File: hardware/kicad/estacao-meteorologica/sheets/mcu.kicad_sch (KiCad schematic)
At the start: 1 part, among them U5 NUCLEO-F446RE

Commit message: refatoracao: atualizacoes de hardware e falta revisao LoRa
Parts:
- removed U5: NUCLEO-F446RE, myLibrary:MODULE_NUCLEO-F446RE, symbol Hardware_MCU:NUCLEO-F446RE_Morpho
- added BT1: Battery_Cell, symbol Device:Battery_Cell
- added C13, C14, C23, C24, C4, C5: 100n, symbol Device:C
- added C15, C16: 4.7u, symbol Device:C
- added C17: 1u, symbol Device:C
- added C18: 10n, symbol Device:C
- added C19, C20, C21, C22: 15pF, symbol Device:C
- added FB1: FerriteBead, symbol Device:FerriteBead
- added J1: Conn_01x02_Pin, symbol Connector:Conn_01x02_Pin
- added J2: Conn_01x06_Pin, symbol Connector:Conn_01x06_Pin
- added J3: UART DEBUG 3V3, symbol Connector:Conn_01x03_Pin
- added R10, R8: 10k, symbol Device:R
- added R11, R6: 4.7k, symbol Device:R
- added SW1: SW_Push, symbol Switch:SW_Push
- added U4: STM32F446RET6, Package_QFP:LQFP-64_10x10mm_P0.5mm, symbol MCU_ST_STM32F4:STM32F446RETx
- added Y2: Crystal, symbol Device:Crystal
- added Y3: Crystal_GND24, symbol Device:Crystal_GND24
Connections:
- net GND: now also BT1.2 (-), C13.2, C14.2, C15.2, C16.2, C17.2, C18.2, C19.1, C20.1, C21.1, C22.1, C23.2, C24.2, C4.2, C5.2, J2.2 (Pin_2), J3.1 (Pin_1), R10.2, SW1.2, U4.12 (VSSA), U4.18 (VSS), U4.31 (VSS), U4.47 (VSS), U4.63 (VSS), Y3.2, Y3.4
- net Lora_DIO0: now also U4.44 (PA11)
- net Lora_DIO1: now also U4.45 (PA12)
- net Lora_MISO: now also U4.35 (PB14)
- net Lora_MOSI: now also U4.36 (PB15)
- net Lora_NSS: now also U4.33 (PB12)
- net Lora_RST: now also U4.24 (PC4)
- net Lora_SCK: now also U4.34 (PB13)
- net MCU_MOSI: now also U4.23 (PA7)
- net RAIN_PULSE: now also U4.15 (PA1)
- net SD_CS: now also U4.25 (PC5)
- net SD_MISO: now also U4.22 (PA6)
- net SD_SCK: now also U4.21 (PA5)
- net WIND_DIR_ADC: now also U4.14 (PA0)
- net WIND_SPEED_PULSE: now also U4.38 (PC7)
- new net: C22.2, U4.4 (PC15), Y2.1
- new net: C21.2, U4.3 (PC14), Y2.2
- new net: C19.2, U4.5 (PH0), Y3.1
- new net: C20.2, U4.6 (PH1), Y3.3
- new net: C16.1, U4.30 (VCAP_1)
- new net +3V3: C13.1, C14.1, C15.1, C4.1, C5.1, FB1.1, J1.1 (Pin_1), J2.1 (Pin_1), R11.1, R6.1, R8.1, U4.19 (VDD), U4.32 (VDD), U4.48 (VDD), U4.64 (VDD)
- new net BOOT0: J1.2 (Pin_2), R10.1, U4.60 (BOOT0)
- new net DHT_SIG: U4.41 (PA8)
- new net I2C1_SCL: R6.2, U4.58 (PB6)
- new net I2C1_SDA: R11.2, U4.59 (PB7)
- new net NRST: C24.1, J2.5 (Pin_5), R8.2, SW1.1, U4.7 (NRST)
- new net RXD: J3.3 (Pin_3), U4.17 (PA3)
- new net SWCLK: J2.4 (Pin_4), U4.49 (PA14)
- new net SWDIO: J2.3 (Pin_3), U4.46 (PA13)
- new net SWO: J2.6 (Pin_6), U4.55 (PB3)
- new net TXD: J3.2 (Pin_2), U4.16 (PA2)
- new net VBAT: BT1.1 (+), C23.1, U4.1 (VBAT)
- new net VDDA: C17.1, C18.1, FB1.2, U4.13 (VDDA)
- no-connect marks 42 -> 24

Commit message: refatoracao: lora + Verificacao projeto inteiro
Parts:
- BT1: value Battery_Cell -> CR2032 / BS-5 vertical; footprint (none) -> Hardware_MCU:BT_Holder_MPD_BS-5_Vertical; Assembly (none) -> Manual — suporte PTH vertical.; Electrical Parameters (none) -> CR2032/BR2032, 3 V; THT; 3 furos Ø0,9 mm; dois pads + e um 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; Function (none) -> Alimenta VBAT do STM32 para reter o domínio de backup e o R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; LCSC (none) -> C6869743; LCSC Part (none) -> C6869743; MPN (none) -> BS-5; Manufacturer (none) -> MPD (Memory Protection Devices); Modelo 3D (none) -> ${KIPRJMOD}/../../libraries/Hardware_MCU/Hardware_MCU.3dsha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; Status_Ficha (none) -> Conferido com desenho mecânico e STEP oficial do MPD BS-5. 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
- C13, C14, C23, C24, C4, C5: footprint (none) -> Capacitor_SMD:C_0603_1608Metric; LCSC (none) -> C14663; LCSC Part (none) -> C14663; MPN (none) -> CC0603KRX7R9BB104; Manufacturer (none) -> YAGEO; Modelo 3D (none) -> ${KICAD9_3DMODEL_DIR}/Capacitor_SMD.3dshapes/C_0603_1608Met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; Status_Ficha (none) -> Conferido no catalogo em 2026-09-24; verificar estoque ao c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
- C15, C16: footprint (none) -> Capacitor_SMD:C_0805_2012Metric; LCSC (none) -> C7307475; LCSC Part (none) -> C7307475; MPN (none) -> MSAST21GAB5475MTNA01; Manufacturer (none) -> Taiyo Yuden; Modelo 3D (none) -> ${KICAD9_3DMODEL_DIR}/Capacitor_SMD.3dshapes/C_0805_2012Met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; Status_Ficha (none) -> Conferido no catalogo em 2026-09-24; verificar estoque ao c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
- C17: footprint (none) -> Capacitor_SMD:C_0603_1608Metric; LCSC (none) -> C513775; LCSC Part (none) -> C513775; MPN (none) -> CS1608X7R105K250NRB; Manufacturer (none) -> Samwha Capacitor; Modelo 3D (none) -> ${KICAD9_3DMODEL_DIR}/Capacitor_SMD.3dshapes/C_0603_1608Met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; Status_Ficha (none) -> Conferido no catalogo em 2026-09-24; verificar estoque ao c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
- C18: footprint (none) -> Capacitor_SMD:C_0603_1608Metric; LCSC (none) -> C57112; LCSC Part (none) -> C57112; MPN (none) -> 0603B103K500NT; Manufacturer (none) -> FH (Guangdong Fenghua Advanced Tech); Modelo 3D (none) -> ${KICAD9_3DMODEL_DIR}/Capacitor_SMD.3dshapes/C_0603_1608Met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; Status_Ficha (none) -> Conferido no catalogo em 2026-09-24; verificar estoque ao c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
- C19: footprint (none) -> Capacitor_SMD:C_0603_1608Metric; Function (none) -> Capacitor de carga do HSE, entre PH0/OSC_IN e GND.; LCSC (none) -> C107037; LCSC Part (none) -> C107037; MPN (none) -> CC0603JRNPO9BN150; Manufacturer (none) -> YAGEO; Modelo 3D (none) -> ${KICAD9_3DMODEL_DIR}/Capacitor_SMD.3dshapes/C_0603_1608Met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; Status_Ficha (none) -> Conferido com Y3: 15 pF C0G, em par simétrico com C20 para 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
- C20: footprint (none) -> Capacitor_SMD:C_0603_1608Metric; Function (none) -> Capacitor de carga do HSE, entre PH1/OSC_OUT e GND.; LCSC (none) -> C107037; LCSC Part (none) -> C107037; MPN (none) -> CC0603JRNPO9BN150; Manufacturer (none) -> YAGEO; Modelo 3D (none) -> ${KICAD9_3DMODEL_DIR}/Capacitor_SMD.3dshapes/C_0603_1608Met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; Status_Ficha (none) -> Conferido com Y3: 15 pF C0G, em par simétrico com C19 para 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
- C21: value 15pF -> 9pF; footprint (none) -> Capacitor_SMD:C_0603_1608Metric; Function (none) -> Capacitor de carga do LSE, entre PC14/OSC32_IN e GND.; LCSC (none) -> C3877909; LCSC Part (none) -> C3877909; MPN (none) -> AC0603DRNPO9BN9R0; Manufacturer (none) -> YAGEO; Modelo 3D (none) -> ${KICAD9_3DMODEL_DIR}/Capacitor_SMD.3dshapes/C_0603_1608Met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; Status_Ficha (none) -> Escolhido para Y2 de CL 7 pF: C21=C22=9 pF com cerca de 2,5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
- C22: value 15pF -> 9pF; footprint (none) -> Capacitor_SMD:C_0603_1608Metric; Function (none) -> Capacitor de carga do LSE, entre PC15/OSC32_OUT e GND.; LCSC (none) -> C3877909; LCSC Part (none) -> C3877909; MPN (none) -> AC0603DRNPO9BN9R0; Manufacturer (none) -> YAGEO; Modelo 3D (none) -> ${KICAD9_3DMODEL_DIR}/Capacitor_SMD.3dshapes/C_0603_1608Met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; Status_Ficha (none) -> Escolhido para Y2 de CL 7 pF: C21=C22=9 pF com cerca de 2,5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
- FB1: footprint (none) -> Inductor_SMD:L_0603_1608Metric; LCSC (none) -> C14709; LCSC Part (none) -> C14709; MPN (none) -> BLM18PG121SN1D; Manufacturer (none) -> Murata Electronics; Modelo 3D (none) -> ${KICAD9_3DMODEL_DIR}/Inductor_SMD.3dshapes/L_0603_1608Metr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; Status_Ficha (none) -> Conferido no catalogo em 2026-09-24; verificar estoque ao c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
- J1: footprint (none) -> Connector_PinHeader_2.54mm:PinHeader_1x02_P2.54mm_Vertical; Assembly (none) -> Manual - pin header PTH 2,54 mm; LCSC (none) -> C492401; LCSC Part (none) -> C492401; MPN (none) -> PZ254V-11-02P; Manufacturer (none) -> XFCN; Modelo 3D (none) -> ${KICAD9_3DMODEL_DIR}/Connector_PinHeader_2.54mm.3dshapes/P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; Status_Ficha (none) -> Conferido no catalogo em 2026-09-24; verificar estoque ao c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
- J2: footprint (none) -> Connector_PinHeader_2.54mm:PinHeader_1x06_P2.54mm_Vertical; Assembly (none) -> Manual - pin header PTH 2,54 mm; LCSC (none) -> C492405; LCSC Part (none) -> C492405; MPN (none) -> PZ254V-11-06P; Manufacturer (none) -> XFCN; Modelo 3D (none) -> ${KICAD9_3DMODEL_DIR}/Connector_PinHeader_2.54mm.3dshapes/P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; Status_Ficha (none) -> Conferido no catalogo em 2026-09-24; verificar estoque ao c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
- J3: footprint (none) -> Connector_PinHeader_2.54mm:PinHeader_1x03_P2.54mm_Vertical; Assembly (none) -> Manual - pin header PTH 2,54 mm; LCSC (none) -> C492402; LCSC Part (none) -> C492402; MPN (none) -> PZ254V-11-03P; Manufacturer (none) -> XFCN; Modelo 3D (none) -> ${KICAD9_3DMODEL_DIR}/Connector_PinHeader_2.54mm.3dshapes/P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; Status_Ficha (none) -> Conferido no catalogo em 2026-09-24; verificar estoque ao c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
- R10, R8: footprint (none) -> Resistor_SMD:R_0603_1608Metric; LCSC (none) -> C25804; LCSC Part (none) -> C25804; MPN (none) -> 0603WAF1002T5E; Manufacturer (none) -> UNI-ROYAL(Uniroyal Elec); Modelo 3D (none) -> ${KICAD9_3DMODEL_DIR}/Resistor_SMD.3dshapes/R_0603_1608Metr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; Status_Ficha (none) -> Conferido no catalogo em 2026-09-24; verificar estoque ao c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
- R11, R6: footprint (none) -> Resistor_SMD:R_0603_1608Metric; LCSC (none) -> C23162; LCSC Part (none) -> C23162; MPN (none) -> 0603WAF4701T5E; Manufacturer (none) -> UNI-ROYAL(Uniroyal Elec); Modelo 3D (none) -> ${KICAD9_3DMODEL_DIR}/Resistor_SMD.3dshapes/R_0603_1608Metr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; Status_Ficha (none) -> Conferido no catalogo em 2026-09-24; verificar estoque ao c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
- SW1: footprint (none) -> Button_Switch_SMD:SW_SPST_TL3342; LCSC (none) -> C2886898; LCSC Part (none) -> C2886898; MPN (none) -> TL3342F160QG; Manufacturer (none) -> E-Switch; Modelo 3D (none) -> ${KICAD9_3DMODEL_DIR}/Button_Switch_SMD.3dshapes/SW_SPST_TL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; Status_Ficha (none) -> Conferido no catalogo em 2026-09-24; verificar estoque ao c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
- U4: LCSC (none) -> C69336; LCSC Part (none) -> C69336; MPN (none) -> STM32F446RET6; Manufacturer (none) -> STMicroelectronics; Modelo 3D (none) -> ${KICAD9_3DMODEL_DIR}/Package_QFP.3dshapes/LQFP-64_10x10mm_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; Status_Ficha (none) -> Conferido no catalogo em 2026-09-24; verificar estoque ao c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
- Y2: value Crystal -> 32.768 kHz / CL 7 pF; footprint (none) -> Crystal:Crystal_SMD_3215-2Pin_3.2x1.5mm; Electrical Parameters (none) -> 32,768 kHz; CL 7 pF; ±20 ppm; SMD3215-2P.; Fabricante / MPN (none) -> SJK (Shenzhen Crystal Tech) / 7LC32768F07UC; Function (none) -> Referência LSE de baixo consumo do RTC do STM32F446, mantid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; LCSC (none) -> C252399; LCSC Part (none) -> C252399; MPN (none) -> 7LC32768F07UC; Manufacturer (none) -> SJK (Shenzhen Crystal Tech); Modelo 3D (none) -> ${KICAD9_3DMODEL_DIR}/Crystal.3dshapes/Crystal_SMD_3215-2Pi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; Status_Ficha (none) -> Conferido. C21=C22=9 pF visa CL≈7 pF para capacitância para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
- Y3: value Crystal_GND24 -> 8 MHz / CL 10 pF; footprint (none) -> Crystal:Crystal_SMD_3225-4Pin_3.2x2.5mm; Electrical Parameters (none) -> 8 MHz; CL 10 pF; ±10 ppm; SMD3225-4P.; Fabricante / MPN (none) -> Suzhou Liming Elec / 3225-8.00-10-10-10/A; Function (none) -> Referência HSE do STM32F446 (PH0/OSC_IN e PH1/OSC_OUT).; LCSC (none) -> C518154; LCSC Part (none) -> C518154; MPN (none) -> 3225-8.00-10-10-10/A; Manufacturer (none) -> Suzhou Liming Elec; Modelo 3D (none) -> ${KICAD9_3DMODEL_DIR}/Crystal.3dshapes/Crystal_SMD_3225-4Pi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; Status_Ficha (none) -> Conferido. Com C19=C20=15 pF e cerca de 2,5 pF de parasitas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
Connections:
- net Lora_DIO2: now reaches U4.26 (PB0)
- no-connect marks 24 -> 23

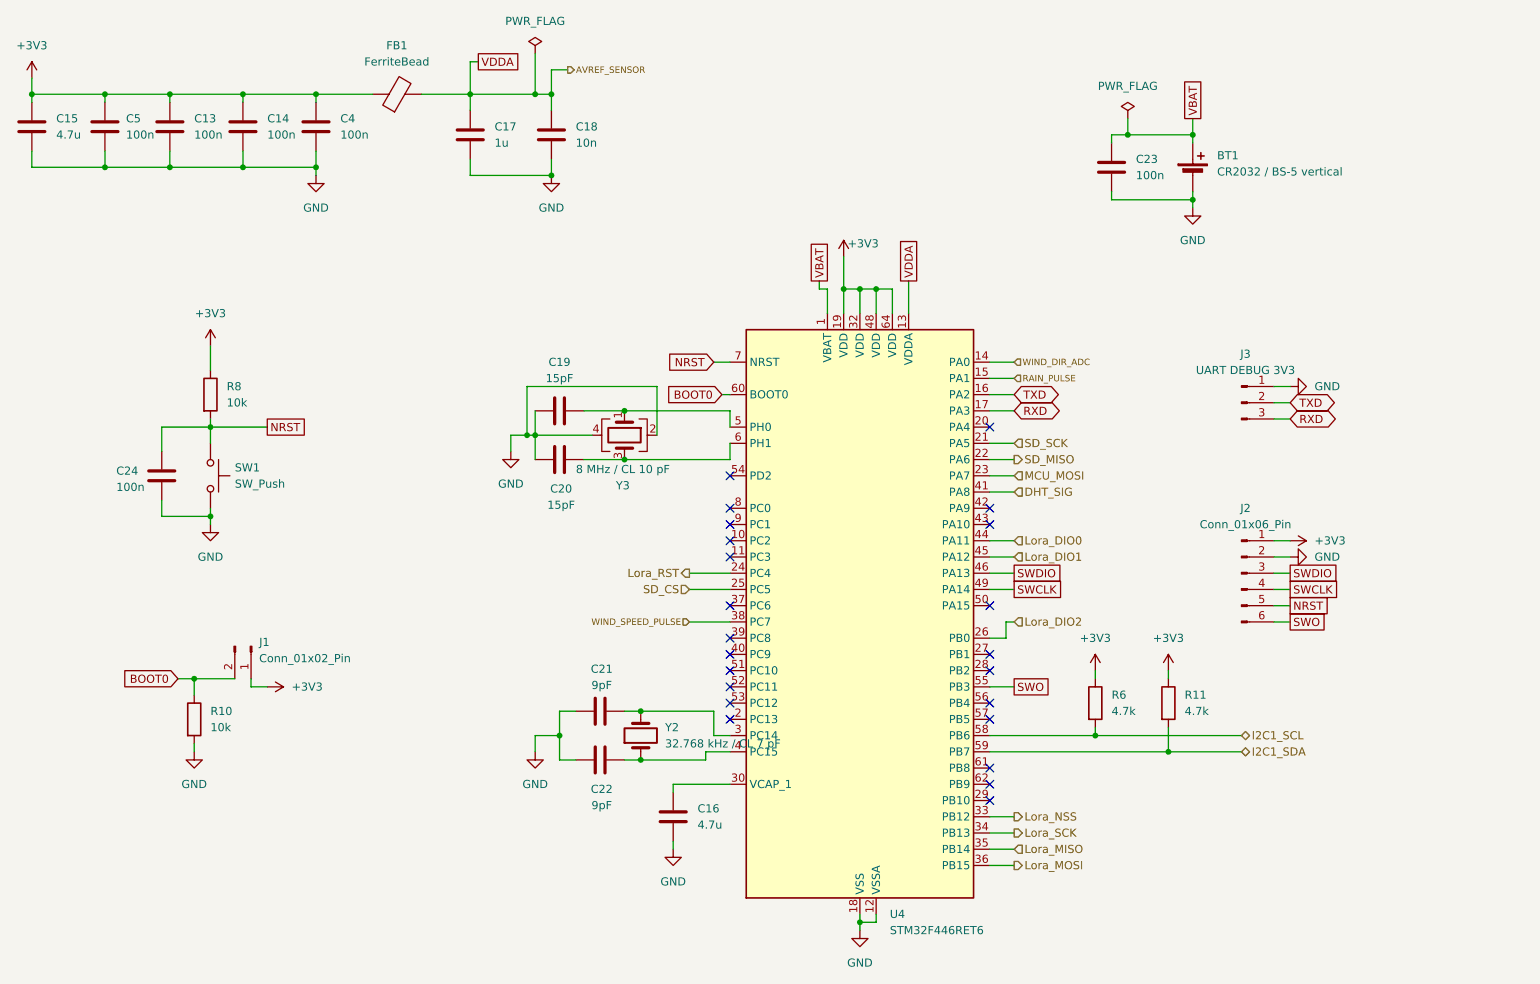
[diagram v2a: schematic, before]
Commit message: Padronizacao de nomes e numero de componentes
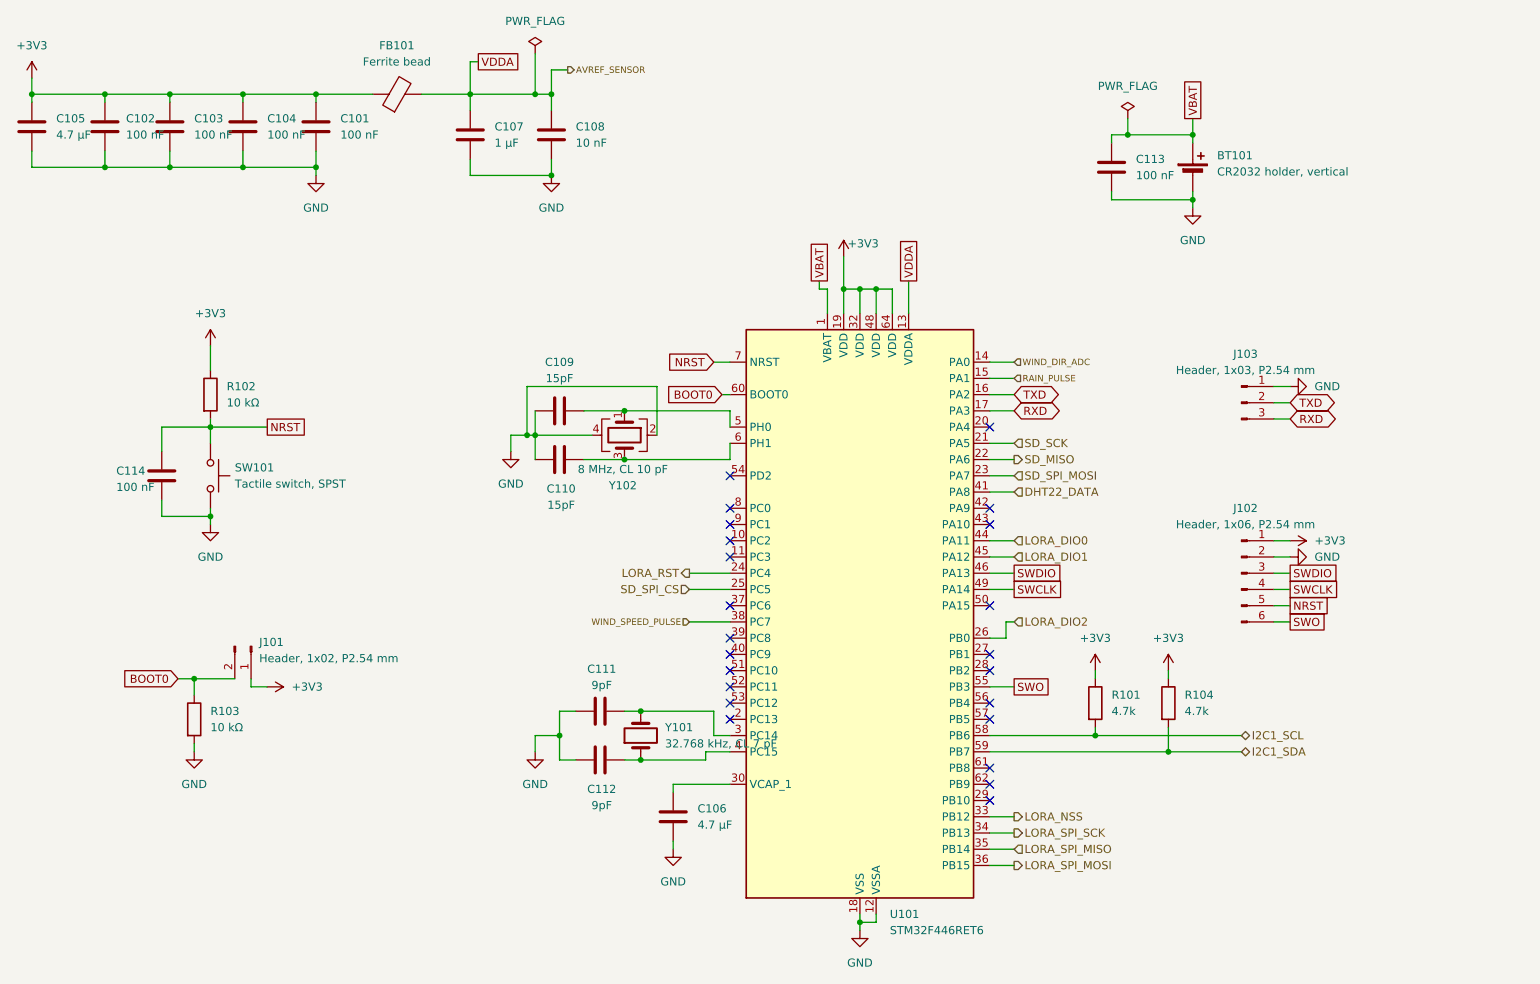
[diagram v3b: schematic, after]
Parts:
- BT101: renamed from BT1; value CR2032 / BS-5 vertical -> CR2032 holder, vertical; Electrical Parameters CR2032/BR2032, 3 V; THT; 3 furos Ø0,9 mm; dois pads + e um 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 -> (none); LCSC Part C6869743 -> (none); Modelo 3D ${KIPRJMOD}/../../libraries/Hardware_MCU/Hardware_MCU.3dsha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 -> (none); Specification (none) -> CR2032/BR2032, 3 V; THT; 3 furos Ø0,9 mm; dois pads + e um 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; Status_Ficha Conferido com desenho mecânico e STEP oficial do MPD BS-5. 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 -> (none); Verification (none) -> Conferido com desenho mecânico e STEP oficial do MPD BS-5. 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
- C101: renamed from C4; value 100n -> 100 nF; Assembly (none) -> SMT; Function (none) -> Capacitor de desacoplamento ou filtro local.; LCSC Part C14663 -> (none); Modelo 3D ${KICAD9_3DMODEL_DIR}/Capacitor_SMD.3dshapes/C_0603_1608Met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 -> (none); Specification (none) -> 100 nF; Status_Ficha Conferido no catalogo em 2026-09-24; verificar estoque ao c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 -> (none); Verification (none) -> Conferido no catalogo em 2026-09-24; verificar estoque ao c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
- C102: renamed from C5; value 100n -> 100 nF; Assembly (none) -> SMT; Function (none) -> Capacitor de desacoplamento ou filtro local.; LCSC Part C14663 -> (none); Modelo 3D ${KICAD9_3DMODEL_DIR}/Capacitor_SMD.3dshapes/C_0603_1608Met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 -> (none); Specification (none) -> 100 nF; Status_Ficha Conferido no catalogo em 2026-09-24; verificar estoque ao c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 -> (none); Verification (none) -> Conferido no catalogo em 2026-09-24; verificar estoque ao c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
- C103: renamed from C13; value 100n -> 100 nF; Assembly (none) -> SMT; Function (none) -> Capacitor de desacoplamento ou filtro local.; LCSC Part C14663 -> (none); Modelo 3D ${KICAD9_3DMODEL_DIR}/Capacitor_SMD.3dshapes/C_0603_1608Met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 -> (none); Specification (none) -> 100 nF; Status_Ficha Conferido no catalogo em 2026-09-24; verificar estoque ao c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 -> (none); Verification (none) -> Conferido no catalogo em 2026-09-24; verificar estoque ao c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
- C104: renamed from C14; value 100n -> 100 nF; Assembly (none) -> SMT; Function (none) -> Capacitor de desacoplamento ou filtro local.; LCSC Part C14663 -> (none); Modelo 3D ${KICAD9_3DMODEL_DIR}/Capacitor_SMD.3dshapes/C_0603_1608Met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 -> (none); Specification (none) -> 100 nF; Status_Ficha Conferido no catalogo em 2026-09-24; verificar estoque ao c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 -> (none); Verification (none) -> Conferido no catalogo em 2026-09-24; verificar estoque ao c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
- C105: renamed from C15; value 4.7u -> 4.7 µF; Assembly (none) -> SMT; Function (none) -> Capacitor de desacoplamento ou filtro local.; LCSC Part C7307475 -> (none); Modelo 3D ${KICAD9_3DMODEL_DIR}/Capacitor_SMD.3dshapes/C_0805_2012Met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 -> (none); Specification (none) -> 4.7 µF; Status_Ficha Conferido no catalogo em 2026-09-24; verificar estoque ao c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 -> (none); Verification (none) -> Conferido no catalogo em 2026-09-24; verificar estoque ao c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
- C106: renamed from C16; value 4.7u -> 4.7 µF; Assembly (none) -> SMT; Function (none) -> Capacitor de desacoplamento ou filtro local.; LCSC Part C7307475 -> (none); Modelo 3D ${KICAD9_3DMODEL_DIR}/Capacitor_SMD.3dshapes/C_0805_2012Met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 -> (none); Specification (none) -> 4.7 µF; Status_Ficha Conferido no catalogo em 2026-09-24; verificar estoque ao c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 -> (none); Verification (none) -> Conferido no catalogo em 2026-09-24; verificar estoque ao c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
- C107: renamed from C17; value 1u -> 1 µF; Assembly (none) -> SMT; Function (none) -> Capacitor de desacoplamento ou filtro local.; LCSC Part C513775 -> (none); Modelo 3D ${KICAD9_3DMODEL_DIR}/Capacitor_SMD.3dshapes/C_0603_1608Met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 -> (none); Specification (none) -> 1 µF; Status_Ficha Conferido no catalogo em 2026-09-24; verificar estoque ao c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 -> (none); Verification (none) -> Conferido no catalogo em 2026-09-24; verificar estoque ao c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
- C108: renamed from C18; value 10n -> 10 nF; Assembly (none) -> SMT; Function (none) -> Capacitor de desacoplamento ou filtro local.; LCSC Part C57112 -> (none); Modelo 3D ${KICAD9_3DMODEL_DIR}/Capacitor_SMD.3dshapes/C_0603_1608Met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 -> (none); Specification (none) -> 10 nF; Status_Ficha Conferido no catalogo em 2026-09-24; verificar estoque ao c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 -> (none); Verification (none) -> Conferido no catalogo em 2026-09-24; verificar estoque ao c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
- C109: renamed from C19; Assembly (none) -> SMT; LCSC Part C107037 -> (none); Modelo 3D ${KICAD9_3DMODEL_DIR}/Capacitor_SMD.3dshapes/C_0603_1608Met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 -> (none); Specification (none) -> 15pF; Status_Ficha Conferido com Y3: 15 pF C0G, em par simétrico com C20 para 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 -> (none); Verification (none) -> Conferido com Y3: 15 pF C0G, em par simétrico com C20 para 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
- C110: renamed from C20; Assembly (none) -> SMT; LCSC Part C107037 -> (none); Modelo 3D ${KICAD9_3DMODEL_DIR}/Capacitor_SMD.3dshapes/C_0603_1608Met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 -> (none); Specification (none) -> 15pF; Status_Ficha Conferido com Y3: 15 pF C0G, em par simétrico com C19 para 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 -> (none); Verification (none) -> Conferido com Y3: 15 pF C0G, em par simétrico com C19 para 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
- C111: renamed from C21; Assembly (none) -> SMT; LCSC Part C3877909 -> (none); Modelo 3D ${KICAD9_3DMODEL_DIR}/Capacitor_SMD.3dshapes/C_0603_1608Met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 -> (none); Specification (none) -> 9pF; Status_Ficha Escolhido para Y2 de CL 7 pF: C21=C22=9 pF com cerca de 2,5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 -> (none); Verification (none) -> Escolhido para Y2 de CL 7 pF: C21=C22=9 pF com cerca de 2,5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
- C112: renamed from C22; Assembly (none) -> SMT; LCSC Part C3877909 -> (none); Modelo 3D ${KICAD9_3DMODEL_DIR}/Capacitor_SMD.3dshapes/C_0603_1608Met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 -> (none); Specification (none) -> 9pF; Status_Ficha Escolhido para Y2 de CL 7 pF: C21=C22=9 pF com cerca de 2,5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 -> (none); Verification (none) -> Escolhido para Y2 de CL 7 pF: C21=C22=9 pF com cerca de 2,5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
- C113: renamed from C23; value 100n -> 100 nF; Assembly (none) -> SMT; Function (none) -> Capacitor de desacoplamento ou filtro local.; LCSC Part C14663 -> (none); Modelo 3D ${KICAD9_3DMODEL_DIR}/Capacitor_SMD.3dshapes/C_0603_1608Met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 -> (none); Specification (none) -> 100 nF; Status_Ficha Conferido no catalogo em 2026-09-24; verificar estoque ao c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 -> (none); Verification (none) -> Conferido no catalogo em 2026-09-24; verificar estoque ao c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
- C114: renamed from C24; value 100n -> 100 nF; Assembly (none) -> SMT; Function (none) -> Capacitor de desacoplamento ou filtro local.; LCSC Part C14663 -> (none); Modelo 3D ${KICAD9_3DMODEL_DIR}/Capacitor_SMD.3dshapes/C_0603_1608Met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 -> (none); Specification (none) -> 100 nF; Status_Ficha Conferido no catalogo em 2026-09-24; verificar estoque ao c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 -> (none); Verification (none) -> Conferido no catalogo em 2026-09-24; verificar estoque ao c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
- FB101: renamed from FB1; value FerriteBead -> Ferrite bead; Assembly (none) -> SMT; Function (none) -> Filtro de ferrite na alimentação.; LCSC Part C14709 -> (none); Modelo 3D ${KICAD9_3DMODEL_DIR}/Inductor_SMD.3dshapes/L_0603_1608Metr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 -> (none); Specification (none) -> Ferrite bead; Status_Ficha Conferido no catalogo em 2026-09-24; verificar estoque ao c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 -> (none); Verification (none) -> Conferido no catalogo em 2026-09-24; verificar estoque ao c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
- J101: renamed from J1; value Conn_01x02_Pin -> Header, 1x02, P2.54 mm; Function (none) -> Conector de interface.; LCSC Part C492401 -> (none); Modelo 3D ${KICAD9_3DMODEL_DIR}/Connector_PinHeader_2.54mm.3dshapes/P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 -> (none); Specification (none) -> Header, 1x02, P2.54 mm; Status_Ficha Conferido no catalogo em 2026-09-24; verificar estoque ao c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 -> (none); Verification (none) -> Conferido no catalogo em 2026-09-24; verificar estoque ao c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
- J102: renamed from J2; value Conn_01x06_Pin -> Header, 1x06, P2.54 mm; Function (none) -> Conector de interface.; LCSC Part C492405 -> (none); Modelo 3D ${KICAD9_3DMODEL_DIR}/Connector_PinHeader_2.54mm.3dshapes/P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 -> (none); Specification (none) -> Header, 1x06, P2.54 mm; Status_Ficha Conferido no catalogo em 2026-09-24; verificar estoque ao c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 -> (none); Verification (none) -> Conferido no catalogo em 2026-09-24; verificar estoque ao c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
- J103: renamed from J3; value UART DEBUG 3V3 -> Header, 1x03, P2.54 mm; Function (none) -> Conector de interface.; LCSC Part C492402 -> (none); Modelo 3D ${KICAD9_3DMODEL_DIR}/Connector_PinHeader_2.54mm.3dshapes/P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 -> (none); Specification (none) -> Header, 1x03, P2.54 mm; Status_Ficha Conferido no catalogo em 2026-09-24; verificar estoque ao c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 -> (none); Verification (none) -> Conferido no catalogo em 2026-09-24; verificar estoque ao c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
- R101: renamed from R6; Assembly (none) -> SMT; Function (none) -> Resistor de polarização, filtro ou configuração.; LCSC Part C23162 -> (none); Modelo 3D ${KICAD9_3DMODEL_DIR}/Resistor_SMD.3dshapes/R_0603_1608Metr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 -> (none); Specification (none) -> 4.7k; Status_Ficha Conferido no catalogo em 2026-09-24; verificar estoque ao c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 -> (none); Verification (none) -> Conferido no catalogo em 2026-09-24; verificar estoque ao c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
- R102: renamed from R8; value 10k -> 10 kΩ; Assembly (none) -> SMT; Function (none) -> Resistor de polarização, filtro ou configuração.; LCSC Part C25804 -> (none); Modelo 3D ${KICAD9_3DMODEL_DIR}/Resistor_SMD.3dshapes/R_0603_1608Metr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 -> (none); Specification (none) -> 10 kΩ; Status_Ficha Conferido no catalogo em 2026-09-24; verificar estoque ao c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 -> (none); Verification (none) -> Conferido no catalogo em 2026-09-24; verificar estoque ao c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
- R103: renamed from R10; value 10k -> 10 kΩ; Assembly (none) -> SMT; Function (none) -> Resistor de polarização, filtro ou configuração.; LCSC Part C25804 -> (none); Modelo 3D ${KICAD9_3DMODEL_DIR}/Resistor_SMD.3dshapes/R_0603_1608Metr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 -> (none); Specification (none) -> 10 kΩ; Status_Ficha Conferido no catalogo em 2026-09-24; verificar estoque ao c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 -> (none); Verification (none) -> Conferido no catalogo em 2026-09-24; verificar estoque ao c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
- R104: renamed from R11; Assembly (none) -> SMT; Function (none) -> Resistor de polarização, filtro ou configuração.; LCSC Part C23162 -> (none); Modelo 3D ${KICAD9_3DMODEL_DIR}/Resistor_SMD.3dshapes/R_0603_1608Metr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 -> (none); Specification (none) -> 4.7k; Status_Ficha Conferido no catalogo em 2026-09-24; verificar estoque ao c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 -> (none); Verification (none) -> Conferido no catalogo em 2026-09-24; verificar estoque ao c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
- SW101: renamed from SW1; value SW_Push -> Tactile switch, SPST; Assembly (none) -> SMT; Function (none) -> Chave/botão de interface local.; LCSC Part C2886898 -> (none); Modelo 3D ${KICAD9_3DMODEL_DIR}/Button_Switch_SMD.3dshapes/SW_SPST_TL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 -> (none); Specification (none) -> Tactile switch, SPST; Status_Ficha Conferido no catalogo em 2026-09-24; verificar estoque ao c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 -> (none); Verification (none) -> Conferido no catalogo em 2026-09-24; verificar estoque ao c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
- U101: renamed from U4; Assembly (none) -> SMT; Function (none) -> Circuito integrado ou módulo funcional.; LCSC Part C69336 -> (none); Modelo 3D ${KICAD9_3DMODEL_DIR}/Package_QFP.3dshapes/LQFP-64_10x10mm_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 -> (none); Specification (none) -> STM32F446RET6; Status_Ficha Conferido no catalogo em 2026-09-24; verificar estoque ao c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 -> (none); Verification (none) -> Conferido no catalogo em 2026-09-24; verificar estoque ao c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
- Y101: renamed from Y2; value 32.768 kHz / CL 7 pF -> 32.768 kHz, CL 7 pF; Assembly (none) -> SMT; Electrical Parameters 32,768 kHz; CL 7 pF; ±20 ppm; SMD3215-2P. -> (none); Fabricante / MPN SJK (Shenzhen Crystal Tech) / 7LC32768F07UC -> (none); LCSC Part C252399 -> (none); Modelo 3D ${KICAD9_3DMODEL_DIR}/Crystal.3dshapes/Crystal_SMD_3215-2Pi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 -> (none); Specification (none) -> 32,768 kHz; CL 7 pF; ±20 ppm; SMD3215-2P.; Status_Ficha Conferido. C21=C22=9 pF visa CL≈7 pF para capacitância para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 -> (none); Verification (none) -> Conferido. C21=C22=9 pF visa CL≈7 pF para capacitância para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
- Y102: renamed from Y3; value 8 MHz / CL 10 pF -> 8 MHz, CL 10 pF; Assembly (none) -> SMT; Electrical Parameters 8 MHz; CL 10 pF; ±10 ppm; SMD3225-4P. -> (none); Fabricante / MPN Suzhou Liming Elec / 3225-8.00-10-10-10/A -> (none); LCSC Part C518154 -> (none); Modelo 3D ${KICAD9_3DMODEL_DIR}/Crystal.3dshapes/Crystal_SMD_3225-4Pi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 -> (none); Specification (none) -> 8 MHz; CL 10 pF; ±10 ppm; SMD3225-4P.; Status_Ficha Conferido. Com C19=C20=15 pF e cerca de 2,5 pF de parasitas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 -> (none); Verification (none) -> Conferido. Com C19=C20=15 pF e cerca de 2,5 pF de parasitas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
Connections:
- net DHT_SIG renamed DHT22_DATA
- net Lora_DIO0 renamed LORA_DIO0
- net Lora_DIO1 renamed LORA_DIO1
- net Lora_DIO2 renamed LORA_DIO2
- net Lora_MISO renamed LORA_SPI_MISO
- net Lora_MOSI renamed LORA_SPI_MOSI
- net Lora_NSS renamed LORA_NSS
- net Lora_RST renamed LORA_RST
- net Lora_SCK renamed LORA_SPI_SCK
- net MCU_MOSI renamed SD_SPI_MOSI
- net SD_CS renamed SD_SPI_CS

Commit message: Ajuste de componentes por folha
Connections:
- net VDDA renamed AVREF_SENSOR
